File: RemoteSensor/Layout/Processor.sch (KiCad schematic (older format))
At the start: 22 parts, among them J3 LCD_HEADER, J4 PRG_HEADER, Q3 2N7002, U7 ESP-12F, U8 LM50CIM3, U9 MCP23008-E_P

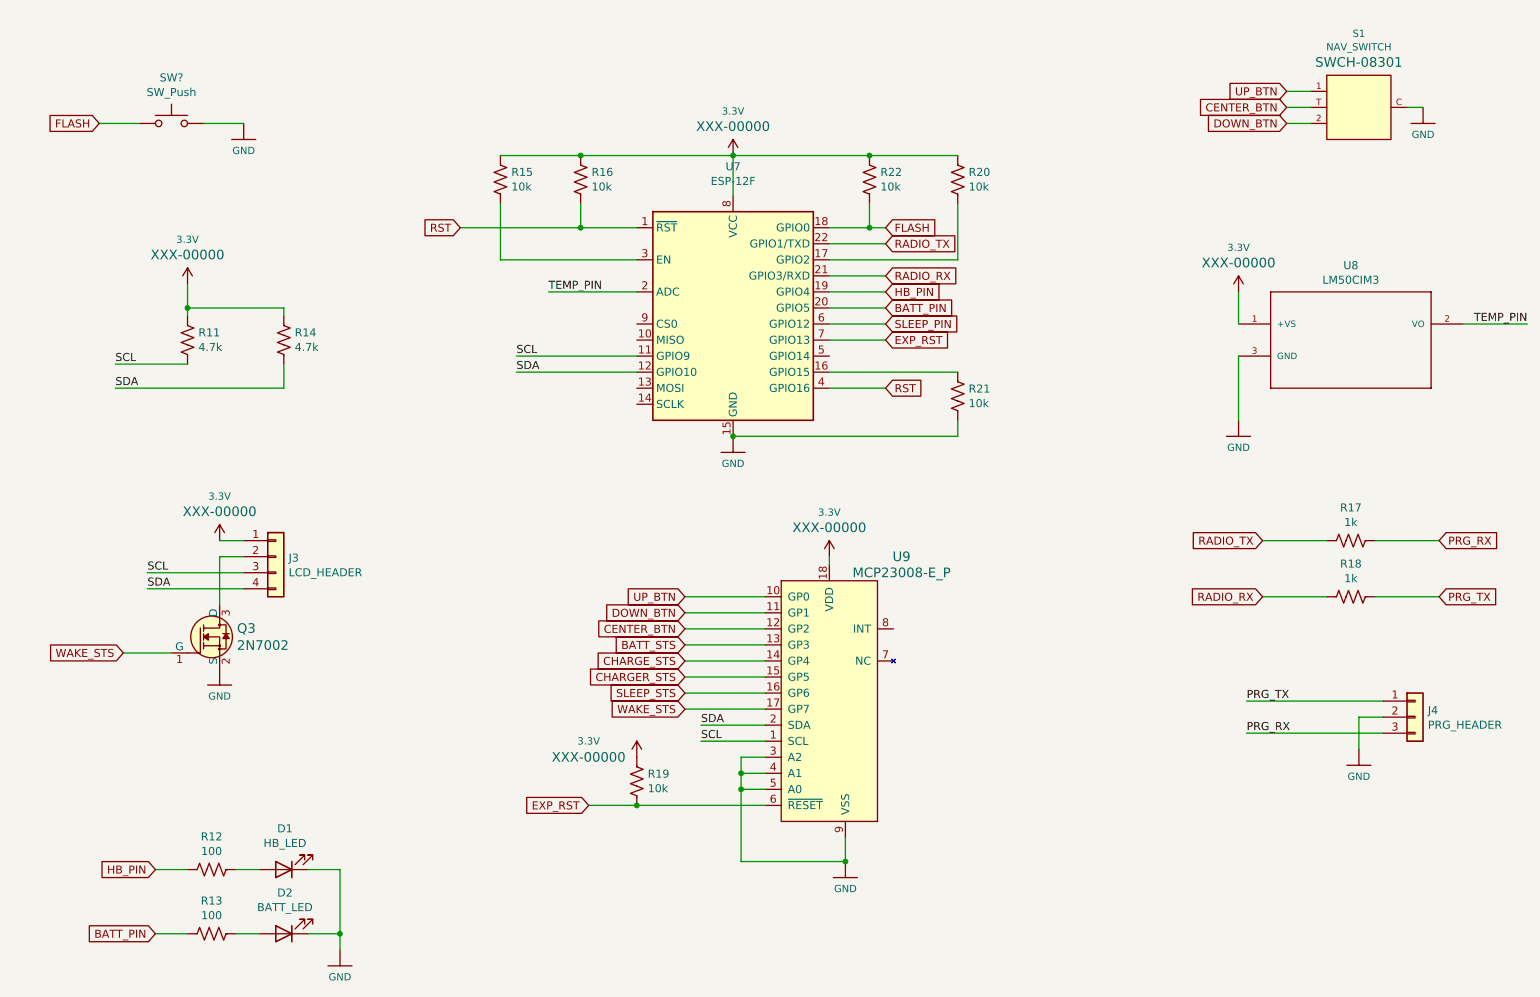
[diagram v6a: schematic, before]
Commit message: Change the USB switching regulator for an LDO
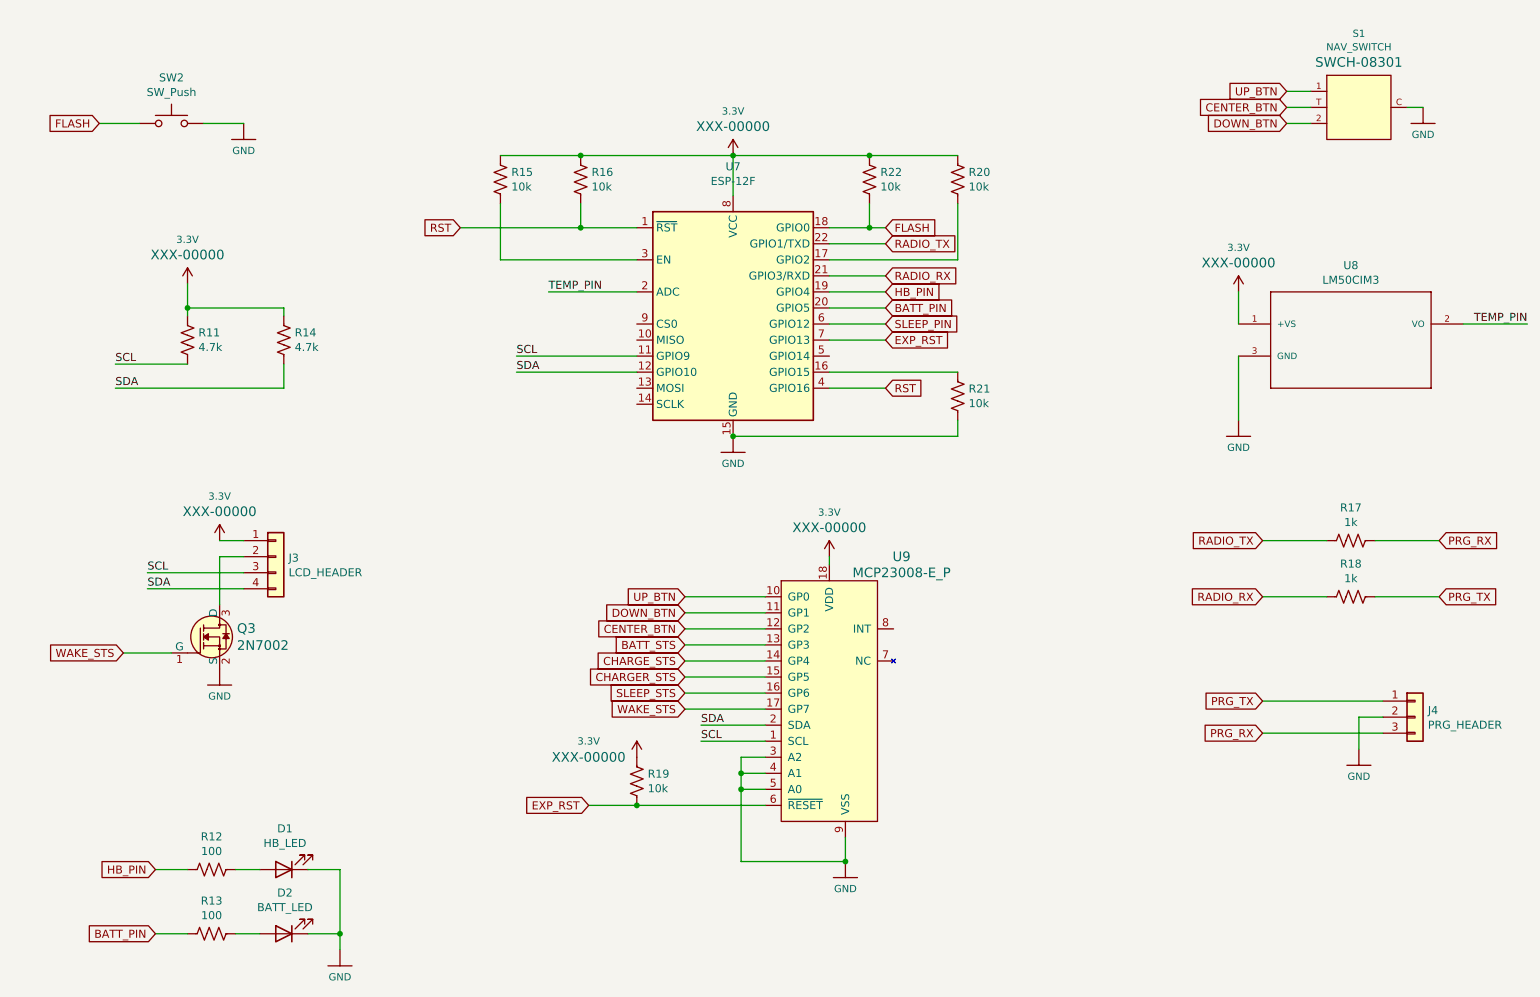
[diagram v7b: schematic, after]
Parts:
- gave numbers to parts that had none: 1
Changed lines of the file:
@@
 Wire Wire Line
 	9650 5000 9500 5000
-Wire Wire Line
-	9500 5000 9500 5200
-Text Label 8800 4900 0    50   ~ 0
-PRG_TX
-Text Label 8800 5100 0    50   ~ 0
-PRG_RX
 $Comp
 L Device:R_US R?
@@
 Wire Wire Line
 	6200 2950 6550 2950
-Wire Wire Line
-	8800 4900 9650 4900
-Wire Wire Line
-	8800 5100 9650 5100
 Wire Wire Line
 	6300 5750 6300 5900
@@
 DOWN_BTN
 $Comp
-L Switch:SW_Push SW?
+L Switch:SW_Push SW2
 U 1 1 5EF8556A
 P 2100 1300
-F 0 "SW?" H 2100 1585 50  0000 C CNN
+F 0 "SW2" H 2100 1585 50  0000 C CNN
 F 1 "SW_Push" H 2100 1494 50  0000 C CNN
 F 2 "Button_Switch_SMD:SW_SPST_TL3342" H 2100 1500 50  0001 C CNN
@@
 $EndComp
 $Comp
-L SparkFun-PowerSymbols:GND #GND?
+L SparkFun-PowerSymbols:GND #GND0123
 U 1 1 5EF95E82
 P 2550 1300
-F 0 "#GND?" H 2600 1250 45  0001 L BNN
+F 0 "#GND0123" H 2600 1250 45  0001 L BNN
 F 1 "GND" H 2550 1130 45  0000 C CNN
 F 2 "" H 2550 1200 60  0001 C CNN
@@
 Wire Wire Line
 	1650 1300 1900 1300
+Text GLabel 8900 4900 0    50   Input ~ 0
+PRG_TX
+Text GLabel 8900 5100 0    50   Input ~ 0
+PRG_RX
+Wire Wire Line
+	8900 5100 9650 5100
+Wire Wire Line
+	8900 4900 9650 4900
+Wire Wire Line
+	9500 5000 9500 5200
 $EndSCHEMATC

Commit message: Update PCB layout
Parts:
- removed J4: PRG_HEADER, Connector_PinSocket_2.54mm:PinSocket_1x03_P2.54mm_Vertical, symbol Connector_Generic:Conn_01x03
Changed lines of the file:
@@
 	8750 2750 8750 3150
-$Comp
-L Connector_Generic:Conn_01x03 J?
-U 1 1 5EF7CD16
-P 9850 5000
-AR Path="/5EF7CD16" Ref="J?"  Part="1"
-AR Path="/5EF5F91F/5EF7CD16" Ref="J4"  Part="1"
-F 0 "J4" H 9930 5042 50  0000 L CNN
-F 1 "PRG_HEADER" H 9930 4951 50  0000 L CNN
-F 2 "Connector_PinSocket_2.54mm:PinSocket_1x03_P2.54mm_Vertical" H 9850 5000 50  0001 C CNN
-F 3 "~" H 9850 5000 50  0001 C CNN
-	1    9850 5000
-	1    0    0    -1
-$EndComp
-$Comp
-L RemoteSensor-rescue:GND-SparkFun-PowerSymbols #GND?
-U 1 1 5EF7CD1C
-P 9500 5200
-AR Path="/5EF7CD1C" Ref="#GND?"  Part="1"
-AR Path="/5EF5F91F/5EF7CD1C" Ref="#GND0120"  Part="1"
-F 0 "#GND0120" H 9550 5150 45  0001 L BNN
-F 1 "GND" H 9500 5030 45  0000 C CNN
-F 2 "" H 9500 5100 60  0001 C CNN
-F 3 "" H 9500 5100 60  0001 C CNN
-	1    9500 5200
-	1    0    0    -1
-$EndComp
-Wire Wire Line
-	9650 5000 9500 5000
 $Comp
 L Device:R_US R?
@@
 Wire Wire Line
 	1650 1300 1900 1300
-Text GLabel 8900 4900 0    50   Input ~ 0
-PRG_TX
-Text GLabel 8900 5100 0    50   Input ~ 0
-PRG_RX
-Wire Wire Line
-	8900 5100 9650 5100
-Wire Wire Line
-	8900 4900 9650 4900
-Wire Wire Line
-	9500 5000 9500 5200
 $EndSCHEMATC
